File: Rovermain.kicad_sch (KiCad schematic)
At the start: 52 parts, among them J1 48V input, J10 12V output, J11 5V output, J12 3V3 output, J13 Steering Bus Bar, J14 Drive Bus Bar, J15 Arm Bus Bar, J16 Pi_48V_Ctrl, J17 Spare 48V port, J2 USB_C_Receptacle_Pi_Power, J3 6-pin JST-GH, J4 USB_C_Receptacle_Spare_power, J5 Buck 48/24, J6 Buck 24/12, J7 Buck 24/5, J8 Buck 12/3v3, J9 24V output, Q1 Arm ctrl, Q2 Steer ctrl, Q3 Drive ctrl, Q4 Spare ctrl, SW1 SW_Push

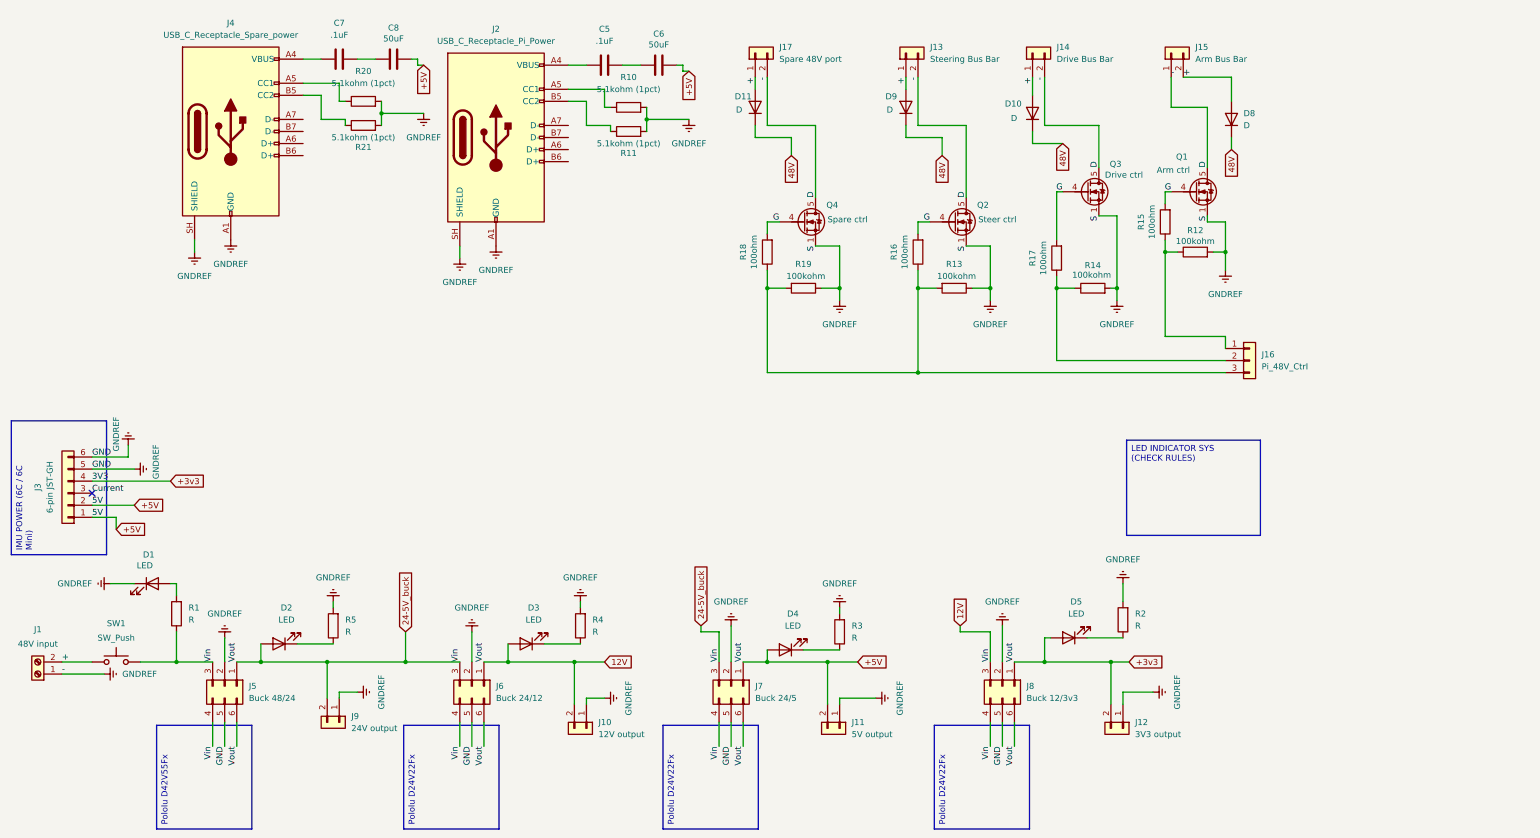
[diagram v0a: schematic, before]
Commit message: added 24V ethernet power
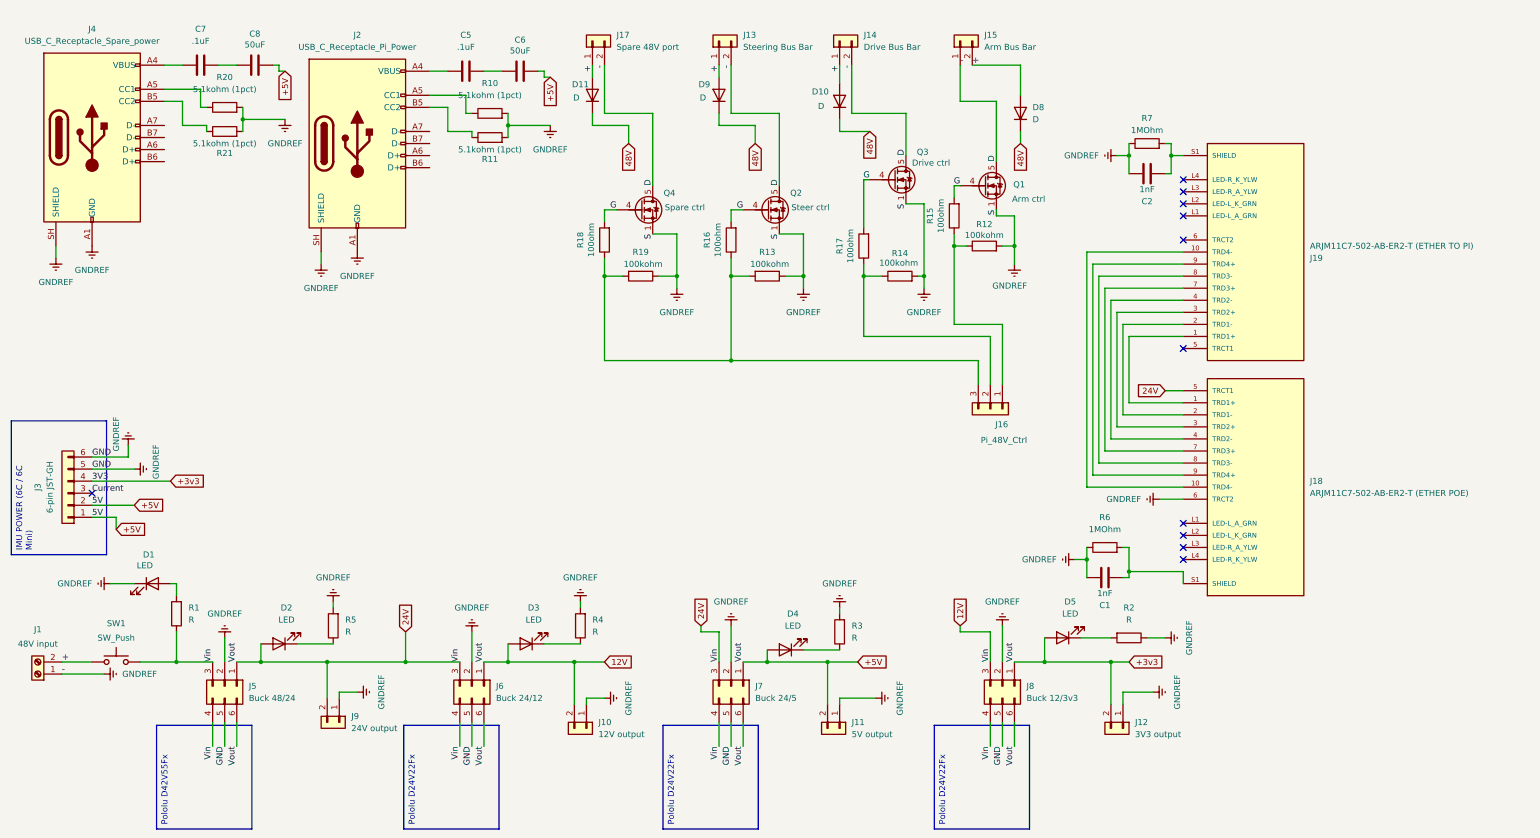
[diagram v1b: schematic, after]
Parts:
- added C1, C2: 1nF, symbol Device:C
- added J18: ARJM11C7-502-AB-ER2-T (ETHER POE), ARJM11C7-502-AB-ER2-T:ABRACON_ARJM11C7-502-AB-ER2-T, symbol ARJM11C7-502-AB-ER2-T:ARJM11C7-502-AB-ER2-T
- added J19: ARJM11C7-502-AB-ER2-T (ETHER TO PI), ARJM11C7-502-AB-ER2-T:ABRACON_ARJM11C7-502-AB-ER2-T, symbol ARJM11C7-502-AB-ER2-T:ARJM11C7-502-AB-ER2-T
- added R6, R7: 1MOhm, Package_DIP:DIP-8_W7.62mm, symbol Device:R
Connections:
- net +3v3: now also J18.5 (TRCT1)
- net GNDREF: now also R2.1, C1.2, C2.2, J18.6 (TRCT2), R6.1, R7.1; no longer R2.2
- net at D5.1 (K): now also R2.2; no longer R2.1
- new net: J18.1 (TRD1+), J19.1 (TRD1+)
- new net: J18.10 (TRD4-), J19.10 (TRD4-)
- new net: J18.2 (TRD1-), J19.2 (TRD1-)
- new net: J18.3 (TRD2+), J19.3 (TRD2+)
- new net: J18.4 (TRD2-), J19.4 (TRD2-)
- new net: J18.7 (TRD3+), J19.7 (TRD3+)
- new net: J18.8 (TRD3-), J19.8 (TRD3-)
- new net: J18.9 (TRD4+), J19.9 (TRD4+)
- new net: C1.1, J18.S1 (SHIELD), J18.S2 (SHIELD), R6.2
- new net: C2.1, J19.S1 (SHIELD), J19.S2 (SHIELD), R7.2
- no-connect marks 1 -> 11
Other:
- moved on the sheet: C5, C6, C7, C8, D10, D11, D5, D8, D9, J13, J14, J15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

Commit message: added fuses
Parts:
- removed J3: 6-pin JST-GH, symbol Connector_Generic:Conn_01x06
- removed SW1: SW_Push, Package_DFN_QFN:Texas_RVA_VQFN-16-1EP_3.5x3.5mm_P0.5mm_EP2.14x2.14mm_ThermalVias, symbol Switch:SW_Push
- added F10, F6, F7, F8, F9: Fuse, symbol Device:Fuse
- added SW1: SW_Push_Open, Button_Switch_THT:SW_NKK_GW12LJP, symbol Switch:SW_Push_Open
- R1: value R -> 22kOhm
- R2: value R -> 150Ohm
- R3: value R -> 330Ohm
- R4: value R -> 1kOhm
- R5: value R -> 2.7kOhm
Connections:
- net +: now also F6.1
- net +3v3: now also F10.1; no longer C6.1, C8.1, D2.2 (A), D3.2 (A), D4.2 (A), J10.2 (Pin_2), J11.2 (Pin_2), J18.5 (TRCT1), J5.1 (Pin_1), J5.3 (Pin_3), J5.4 (Pin_4), J5.6 (Pin_6), J6.1 (Pin_1), J6.3 (Pin_3), J6.4 (Pin_4), J6.6 (Pin_6), J7.1 (Pin_1), J7.3 (Pin_3), J7.4 (Pin_4), J7.6 (Pin_6), J8.1 (Pin_1), J8.3 (Pin_3), J8.4 (Pin_4), J8.6 (Pin_6), J9.2 (Pin_2), R1.1
- net GNDREF: no longer J5.5 (Pin_5), J6.5 (Pin_5), J7.5 (Pin_5), J8.5 (Pin_5)
- new net: F6.2, SW1.1 (A)
- new net +5V: C6.1, C8.1, D4.2 (A), F9.2, J11.2 (Pin_2)
- new net 12V: D2.2 (A), D3.2 (A), F7.2, F8.2, J10.2 (Pin_2), J18.5 (TRCT1), J5.3 (Pin_3), J5.4 (Pin_4), J6.3 (Pin_3), J6.4 (Pin_4), J7.3 (Pin_3), J7.4 (Pin_4), J8.3 (Pin_3), J8.4 (Pin_4), J9.2 (Pin_2), R1.1, SW1.2 (B)
- new net GND: J5.5 (Pin_5), J6.5 (Pin_5), J7.5 (Pin_5), J8.5 (Pin_5)
- new net Vout: F10.2, F7.1, F8.1, F9.1, J5.1 (Pin_1), J5.6 (Pin_6), J6.1 (Pin_1), J6.6 (Pin_6), J7.1 (Pin_1), J7.6 (Pin_6), J8.1 (Pin_1), J8.6 (Pin_6)
- no-connect marks 11 -> 18
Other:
- moved on the sheet: C1, D1, D2, D3, D4, D5, R1, R2, R3, R4, R5

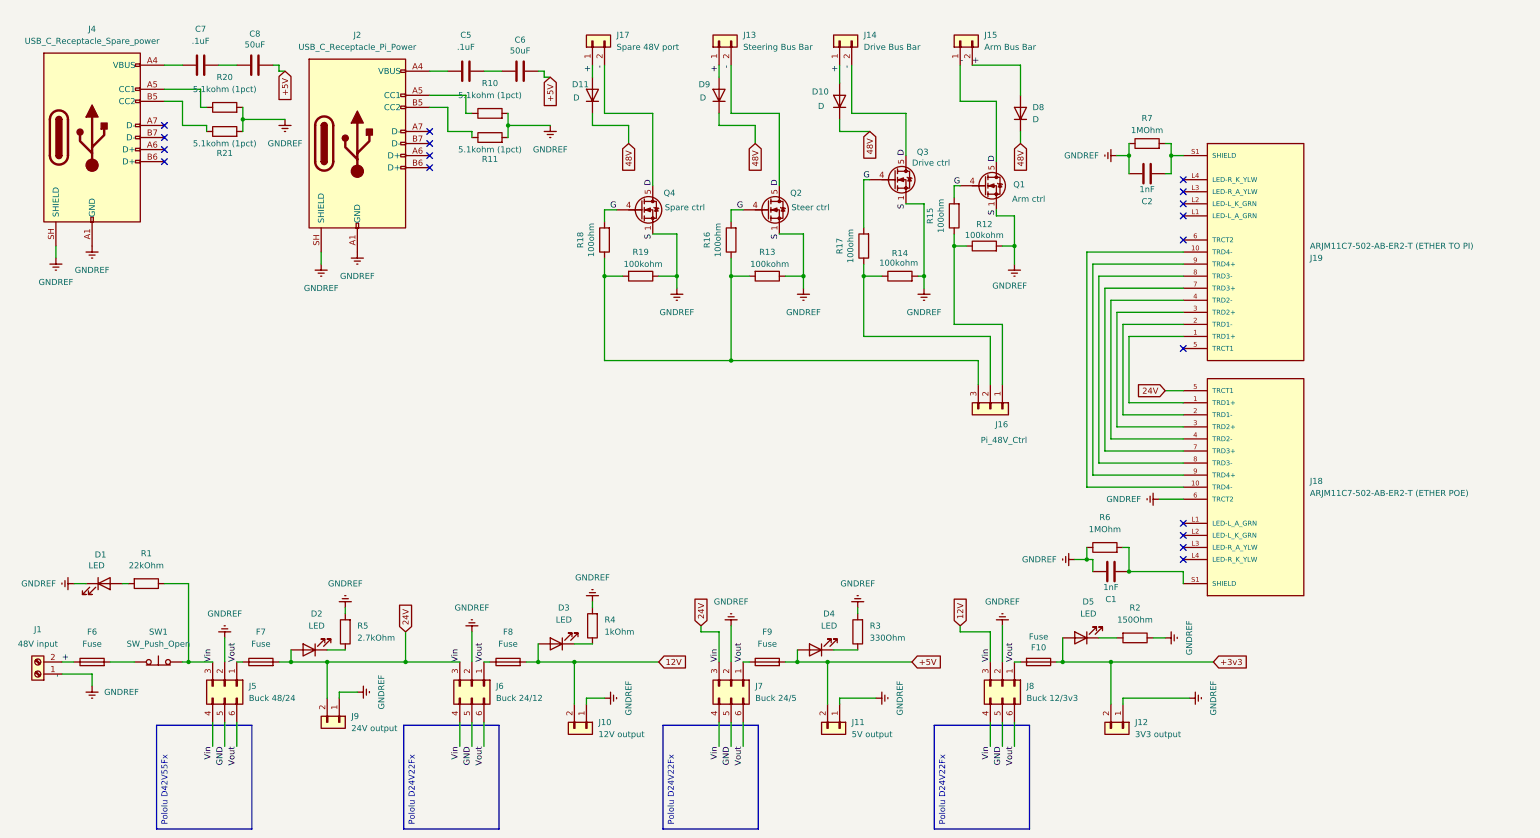
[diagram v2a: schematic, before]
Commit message: overhaul of connectors
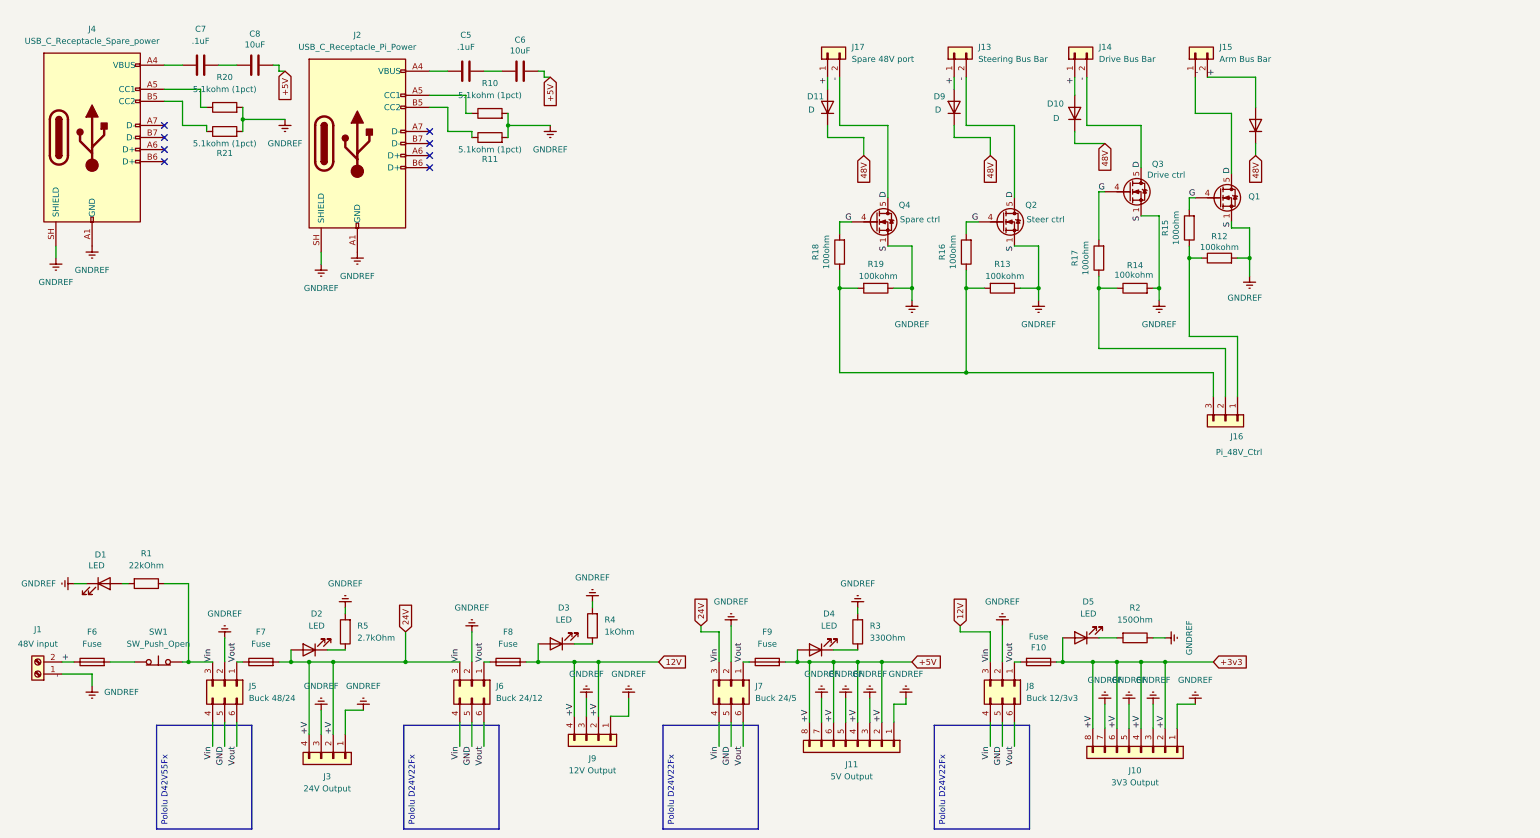
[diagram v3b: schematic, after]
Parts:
- removed C1, C2: 1nF, symbol Device:C
- removed J10: 12V output, Button_Switch_THT:SW_Slide-03_Wuerth-WS-SLTV_10x2.5x6.4_P2.54mm, symbol Connector_Generic:Conn_01x02
- removed J11: 5V output, Button_Switch_THT:SW_Slide-03_Wuerth-WS-SLTV_10x2.5x6.4_P2.54mm, symbol Connector_Generic:Conn_01x02
- removed J12: 3V3 output, Button_Switch_THT:SW_Slide-03_Wuerth-WS-SLTV_10x2.5x6.4_P2.54mm, symbol Connector_Generic:Conn_01x02
- removed J18: ARJM11C7-502-AB-ER2-T (ETHER POE), ARJM11C7-502-AB-ER2-T:ABRACON_ARJM11C7-502-AB-ER2-T, symbol ARJM11C7-502-AB-ER2-T:ARJM11C7-502-AB-ER2-T
- removed J19: ARJM11C7-502-AB-ER2-T (ETHER TO PI), ARJM11C7-502-AB-ER2-T:ABRACON_ARJM11C7-502-AB-ER2-T, symbol ARJM11C7-502-AB-ER2-T:ARJM11C7-502-AB-ER2-T
- removed J9: 24V output, Button_Switch_THT:SW_Slide-03_Wuerth-WS-SLTV_10x2.5x6.4_P2.54mm, symbol Connector_Generic:Conn_01x02
- removed R6, R7: 1MOhm, Package_DIP:DIP-8_W7.62mm, symbol Device:R
- added J10: 3V3 Output, symbol Connector_Generic:Conn_01x08
- added J11: 5V Output, symbol Connector_Generic:Conn_01x08
- added J3: 24V Output, symbol Connector_Generic:Conn_01x04
- added J9: 12V Output, symbol Connector_Generic:Conn_01x04
- C5, C7: footprint (none) -> Capacitor_SMD:C_0603_1608Metric
- C6, C8: value 50uF -> 10uF; footprint (none) -> Capacitor_SMD:C_1206_3216Metric
- J1: footprint Package_SON:WSON-8-1EP_6x5mm_P1.27mm_EP3.4x4mm -> TerminalBlock_Dinkle:TerminalBlock_Dinkle_DT-55-B01X-02_P10.00mm
- R10, R11, R20, R21: footprint Package_DIP:DIP-8_W7.62mm -> Resistor_SMD:R_0402_1005Metric
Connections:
- net +5V is gone; now on net +3v3: C6.1, C8.1, D4.2 (A), F9.2
- net 12V is gone; now on net +3v3: D2.2 (A), D3.2 (A), F7.2, F8.2, J5.3 (Pin_3), J5.4 (Pin_4), J6.3 (Pin_3), J6.4 (Pin_4), J7.3 (Pin_3), J7.4 (Pin_4), J8.3 (Pin_3), J8.4 (Pin_4), R1.1, SW1.2 (B)
- net +3v3: now also J10.2 (Pin_2), J10.4 (Pin_4), J10.6 (Pin_6), J10.8 (Pin_8), J11.2 (Pin_2), J11.4 (Pin_4), J11.6 (Pin_6), J11.8 (Pin_8), J3.2 (Pin_2), J3.4 (Pin_4), J9.2 (Pin_2), J9.4 (Pin_4)
- net GNDREF: now also J10.1 (Pin_1), J10.3 (Pin_3), J10.5 (Pin_5), J10.7 (Pin_7), J11.1 (Pin_1), J11.3 (Pin_3), J11.5 (Pin_5), J11.7 (Pin_7), J3.1 (Pin_1), J3.3 (Pin_3), J9.1 (Pin_1), J9.3 (Pin_3)
- no-connect marks 18 -> 8
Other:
- moved on the sheet: D10, D11, D9, J13, J14, J15, J16, J17, Q1, Q2, Q3, Q4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

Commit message: added relay for emergency shutoff
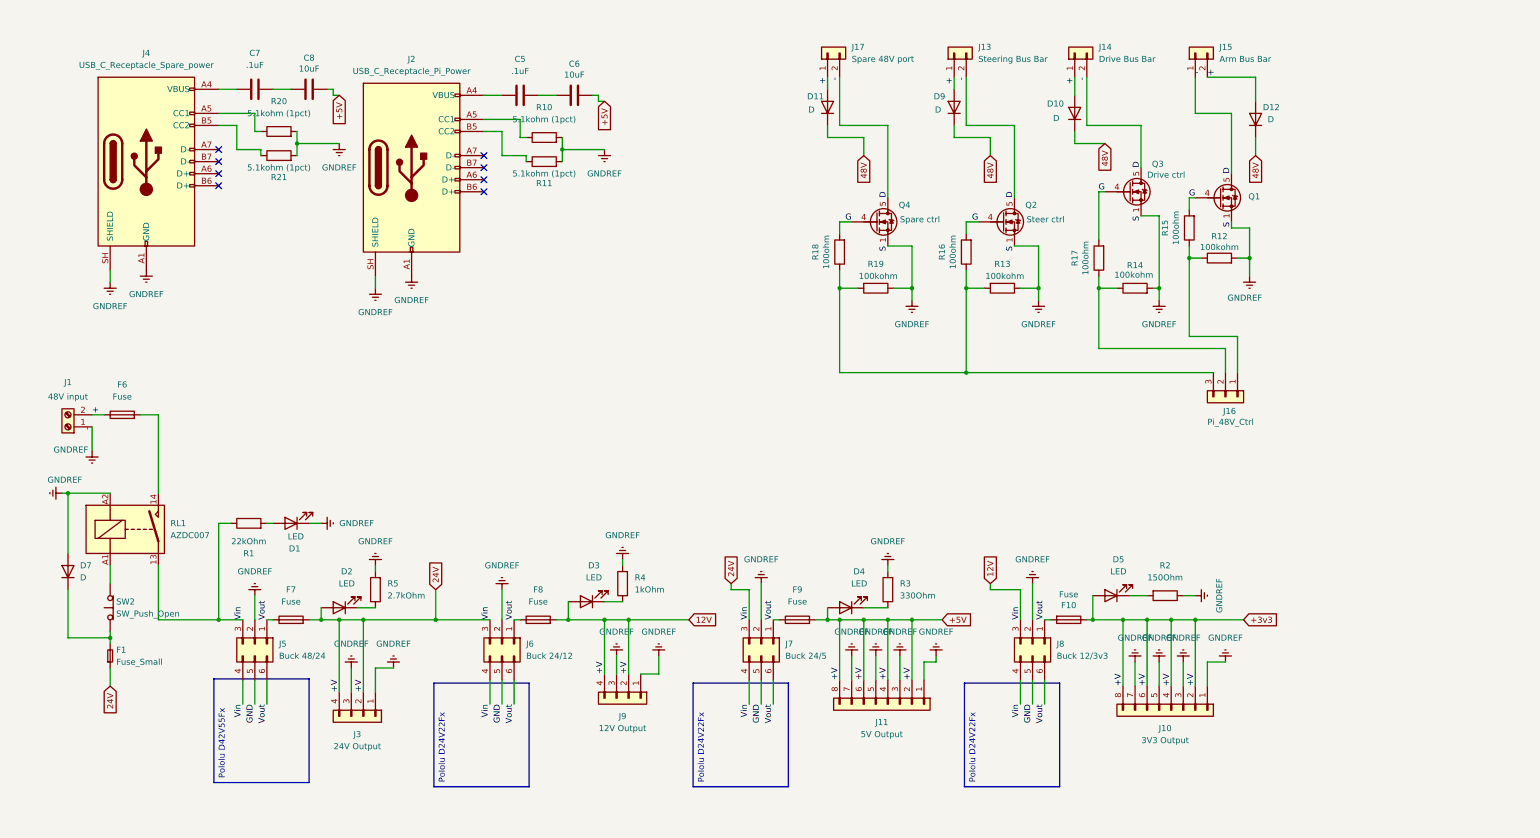
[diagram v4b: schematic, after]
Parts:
- removed D8: D, Diode_THT:D_DO-35_SOD27_P7.62mm_Horizontal, symbol Device:D
- removed SW1: SW_Push_Open, Button_Switch_THT:SW_NKK_GW12LJP, symbol Switch:SW_Push_Open
- added D12, D7: D, SM74611KTTR:TO254P1524X483-3N, symbol Device:D
- added F1: Fuse_Small, symbol Device:Fuse_Small
- added RL1: AZDC007, Relay_THT:Relay_SPST_Zettler-AZSR131, symbol Relay:AZSR131-1AE-12D
- added SW2: SW_Push_Open, Button_Switch_THT:SW_NKK_GW12LJP, symbol Switch:SW_Push_Open
- D10, D11, D9: footprint Diode_THT:D_DO-35_SOD27_P7.62mm_Horizontal -> SM74611KTTR:TO254P1524X483-3N
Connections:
- net +: now also D12.2 (A)
- net +3v3: now also F1.1, RL1.13
- net 48V: now also D12.1 (K)
- net GNDREF: now also D7.2 (A), RL1.A2
- net at F6.2: now also RL1.14
- new net: D7.1 (K), F1.2, SW2.1 (A)
- new net: RL1.A1, SW2.2 (B)
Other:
- moved on the sheet: C5, C6, C7, C8, D1, D2, D3, D4, D5, F10, F6, F7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
